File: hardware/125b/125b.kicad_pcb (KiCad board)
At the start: 2 copper layers, 59 x 75 mm, 51 parts, among them J1 Guitar in, J2 Barrel_Jack, J3 Conn_02x05_Odd_Even_MountingP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, J4 Guitar out, SW1 SW_DIP_x02, SW2 RotaryEncoder_Switch, SW3 Switch 1, SW4 Switch 2, U1 L78L05_TO92, U2 TL074

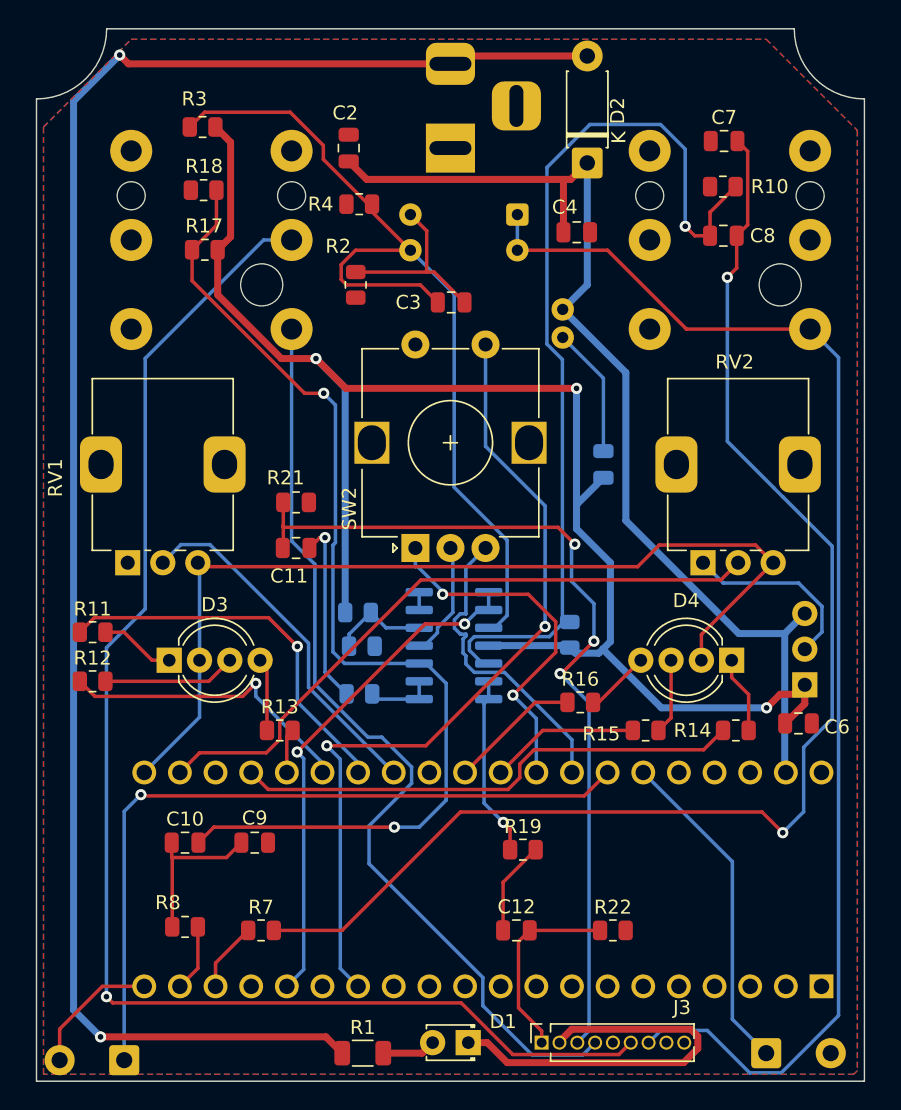
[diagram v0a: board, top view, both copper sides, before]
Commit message: Set up power nets to have wider traces
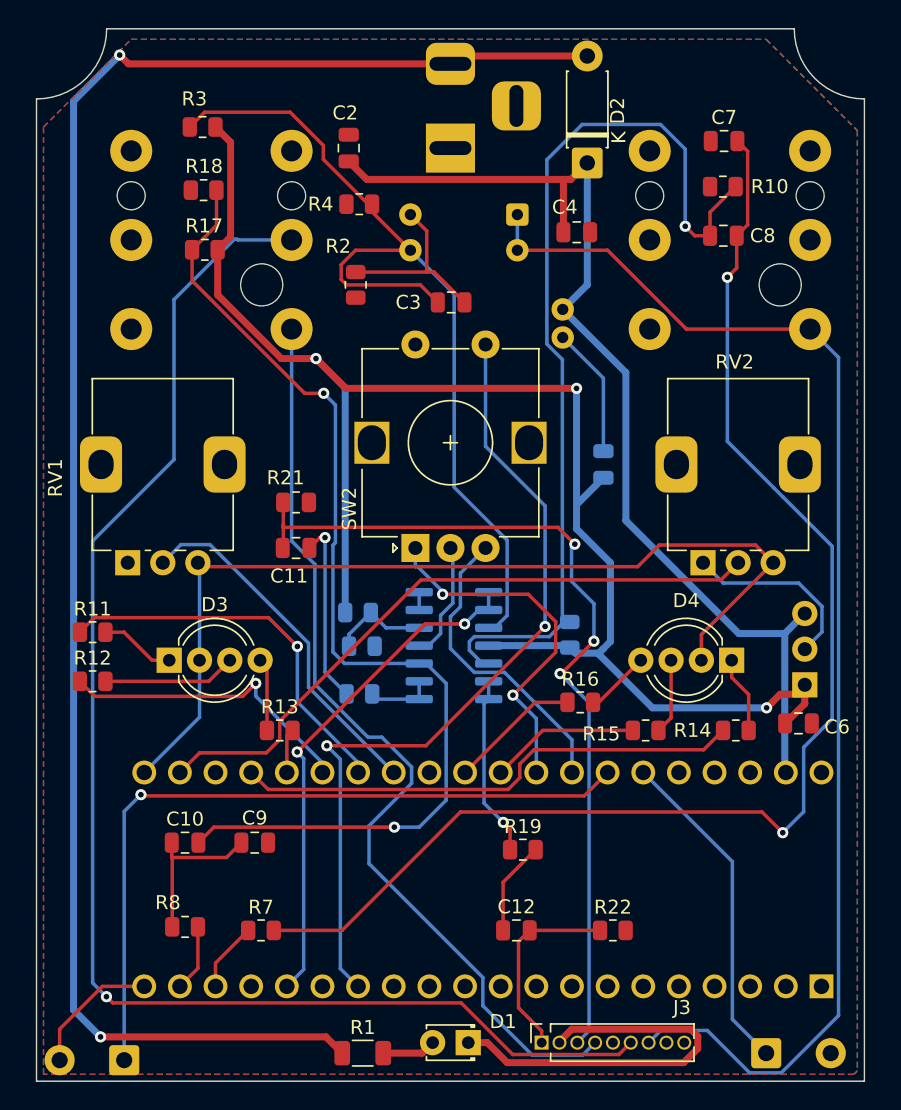
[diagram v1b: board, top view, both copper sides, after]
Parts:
- A1: footprint Library:Electrosmith_Daisy_Seed -> Project:Electrosmith_Daisy_Seed
- J1, J4: footprint Library:Jack_6.35mm_Neutrik_NRJ6HF-1-AU_Horizontal -> Project:Jack_6.35mm_Neutrik_NRJ6HF-1-AU_Horizontal
- U1: footprint Library:TO-92_Inline_Wide_78L05_dc -> Project:TO-92_Inline_Wide_78L05_dc
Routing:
- net /fsw6: track 100.0 -> 102.1 mm

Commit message: All components connected with new IDC socket pos
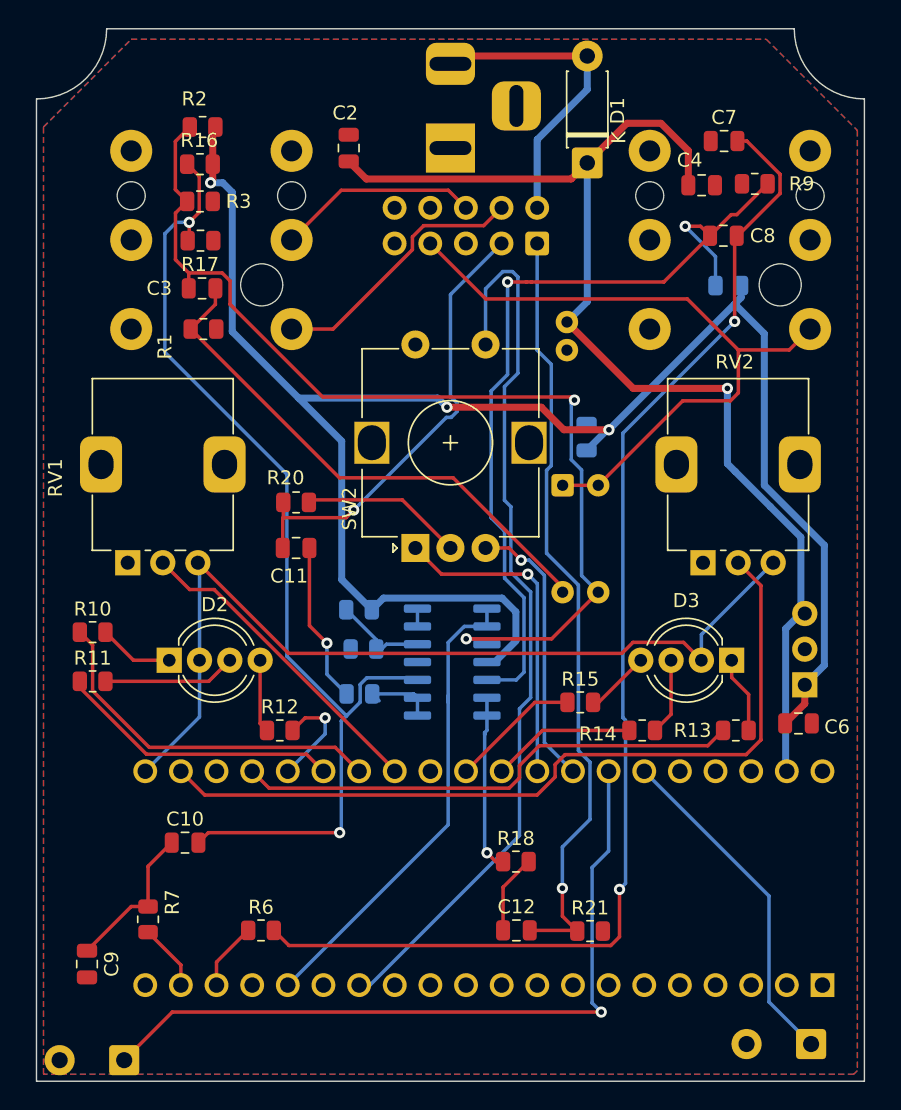
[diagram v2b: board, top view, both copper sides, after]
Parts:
- removed the D1 at (128.8, 107.2)
- removed the R1 at (121.2, 108.0)
- J3: footprint Connector_PinSocket_1.27mm:PinSocket_1x09_P1.27mm_Vertical -> Connector_IDC:IDC-Header_2x05_P2.54mm_Vertical; moved to B.Cu
- moved J3 57.0 mm to (133.7, 50.3)
- moved R8 27.3 mm to (147.3, 53.3), turned to 180 degrees
- moved SW1 19.6 mm to (135.5, 67.5), turned to -90 degrees
- moved C3 17.8 mm to (109.8, 53.5)
- moved C9 14.8 mm to (101.6, 101.7), turned to 90 degrees
- moved R3 11.4 mm to (109.7, 47.3), turned to 0 degrees
- moved R1 11.3 mm to (109.9, 56.4), turned to 0 degrees
- moved C4 9.51 mm to (145.4, 46.1)
- moved R16 6.11 mm to (109.7, 44.6)
- moved R17 3.61 mm to (109.7, 50.1), turned to 0 degrees
- moved SW4 3.27 mm to (153.2, 107.3), turned to 180 degrees
- moved R7 2.69 mm to (106.0, 98.5), turned to 90 degrees
- moved C5 2.29 mm to (137.2, 64.1)
- moved R9 2.28 mm to (149.2, 46.0)
- moved R21 1.63 mm to (137.4, 99.3)
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- renumbered D2 to D1, D3 to D2, D4 to D3, R2 to R1, R11 to R10, R12 to R11, R13 to R12, R14 to R13, R15 to R14, R16 to R15, R17 to R16, R18 to R17, R19 to R18, R20 to R19, R3 to R2, R21 to R20, R22 to R21, R4 to R3, R5 to R4, R6 to R5, R7 to R6, R8 to R7, R9 to R8, R10 to R9
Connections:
- D1 pad 2: Net-(D2-A) -> /fsw2
- J2 pad 2: Net-(D2-A) -> /fsw2
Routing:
- net Net-(D2-A): track 123.6 -> 0.00 mm, vias 2 -> 0
- net /fsw6: track 102.1 -> 14.4 mm, vias 1 -> 0
- net /fsw4: track 66.8 -> 19.1 mm
- net /fsw7: track 92.3 -> 49.1 mm
- net /fsw1: track 14.0 -> 55.5 mm, vias 0 -> 1
- net /fsw3: track 63.1 -> 32.5 mm, vias 3 -> 1
- net GND: track 40.6 -> 11.6 mm
- net Net-(C3-Pad1): track 13.2 -> 38.1 mm
- net +5V: track 111.1 -> 128.7 mm
- net Net-(A1-ADC_0): track 46.7 -> 57.5 mm
- net /VCC: track 76.5 -> 85.2 mm, vias 0 -> 1
- net Net-(U2A-+): track 65.7 -> 72.2 mm, vias 0 -> 2
- net Net-(C7-Pad2): track 95.1 -> 88.6 mm
- net /fsw2: track 28.7 -> 22.3 mm
- net Net-(U2B-+): track 67.0 -> 60.7 mm, vias 1 -> 2
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
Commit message: Move r8 from underneath audio socket
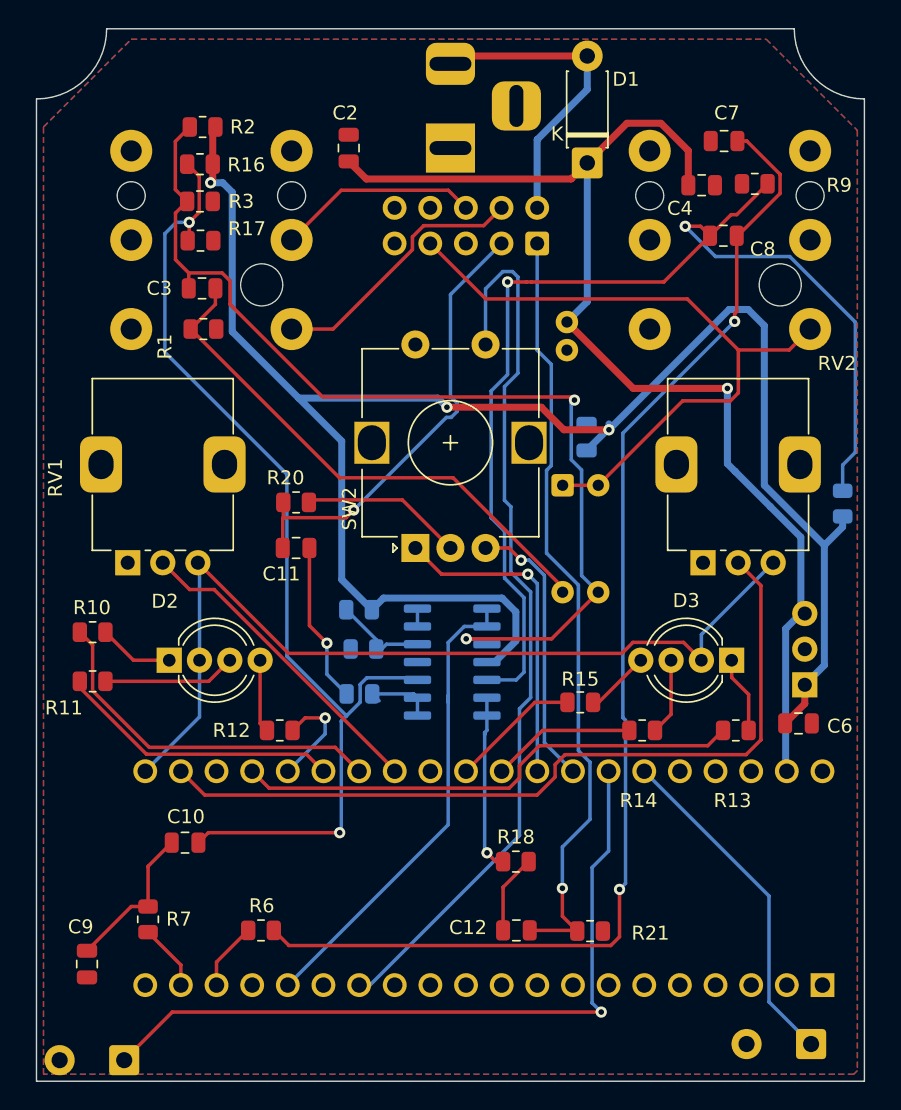
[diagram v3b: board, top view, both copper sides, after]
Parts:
- moved R8 17.5 mm to (155.4, 68.8), turned to 90 degrees
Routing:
- net Net-(U2B-+): track 60.7 -> 83.0 mm
- net +5V: track 128.7 -> 130.2 mm

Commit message: Rotate IDC socket for cleaner ribbon direction
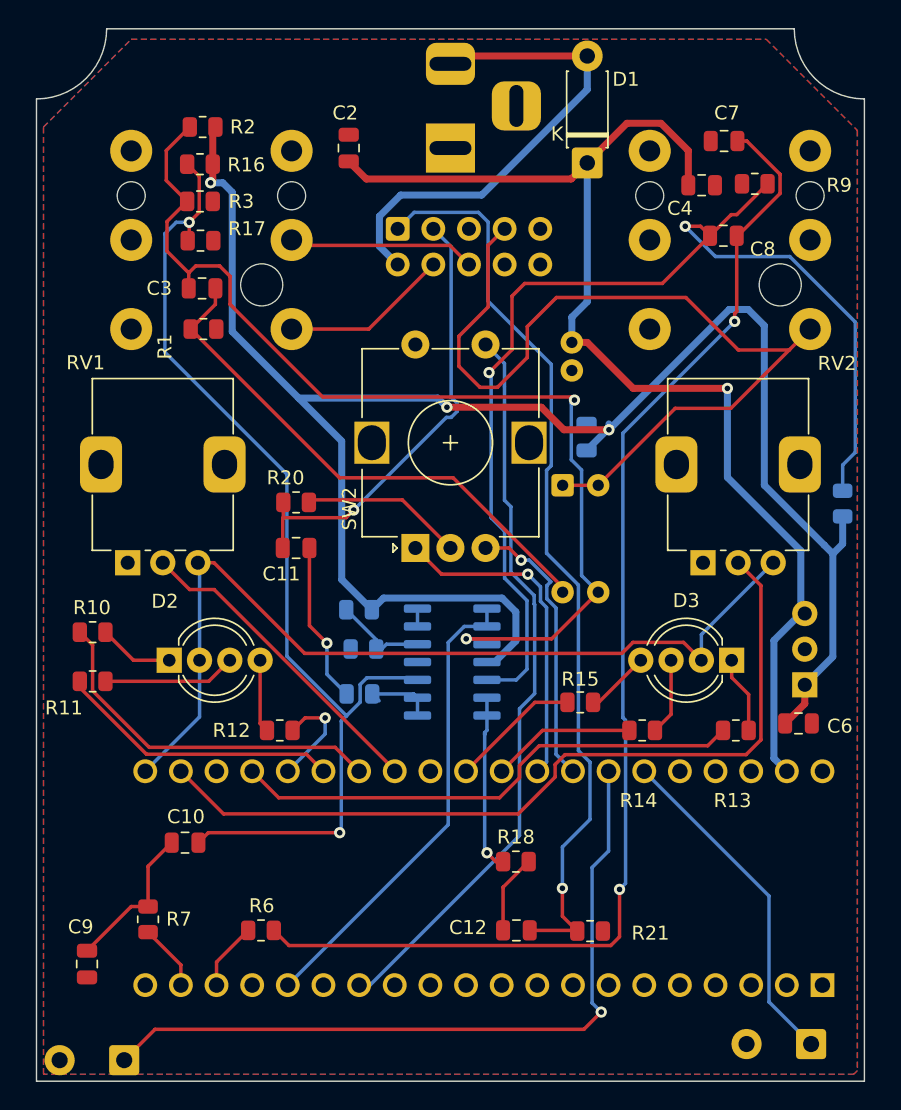
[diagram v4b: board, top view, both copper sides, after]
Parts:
- moved J3 9.99 mm to (123.7, 49.3), turned to -90 degrees
- moved C1 1.49 mm to (136.2, 57.4)
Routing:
- net /fsw7: track 49.1 -> 63.1 mm
- net /fsw2: track 22.3 -> 34.9 mm
- net /ENC_CLICK: track 64.1 -> 52.7 mm
- net /fsw1: track 55.5 -> 65.7 mm
- net /fsw4: track 19.1 -> 12.0 mm
- net Net-(U2A-+): track 72.2 -> 73.9 mm
- net Net-(A1-ADC_0): track 57.5 -> 58.6 mm
- net /VCC: track 85.2 -> 86.2 mm
- net /fsw6: track 14.4 -> 13.4 mm
- net +5V: track 130.2 -> 131.1 mm
- net /LED_2_R: track 36.3 -> 36.8 mm
- net /ENC_A: track 23.1 -> 23.7 mm

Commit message: Adjust switch connector positions and add fiducials
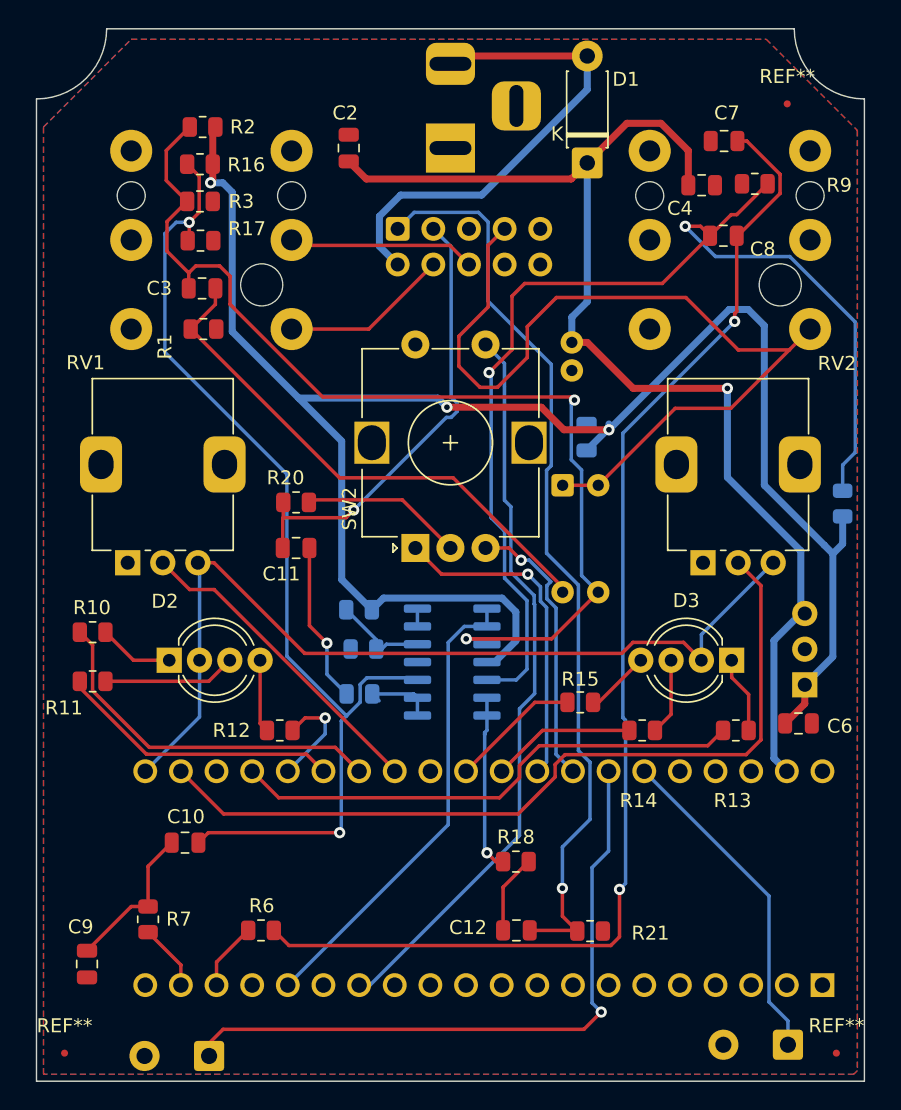
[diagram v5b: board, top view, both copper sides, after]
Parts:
- added REF**: Fiducial_0.5mm_Mask2mm, Fiducial:Fiducial_0.5mm_Mask2mm, F.Cu at (100.0, 108.0)
- added REF**: Fiducial_0.5mm_Mask2mm, Fiducial:Fiducial_0.5mm_Mask2mm, F.Cu at (151.5, 40.4)
- added REF**: Fiducial_0.5mm_Mask2mm, Fiducial:Fiducial_0.5mm_Mask2mm, F.Cu at (155.0, 108.0)
- moved SW3 6.06 mm to (110.3, 108.2)
- moved SW4 1.65 mm to (151.6, 107.4)
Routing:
- net Net-(A1-SAI2_FS): track 53.3 -> 47.7 mm
- net Net-(A1-SAI2_SCK): track 24.4 -> 23.7 mm
